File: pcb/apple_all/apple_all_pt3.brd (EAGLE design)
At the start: 56 x 65 mm, 47 parts, among them IC1 STM32F072C8T6, SW1 324_SW, SW2 324_SW, SW3 324_SW

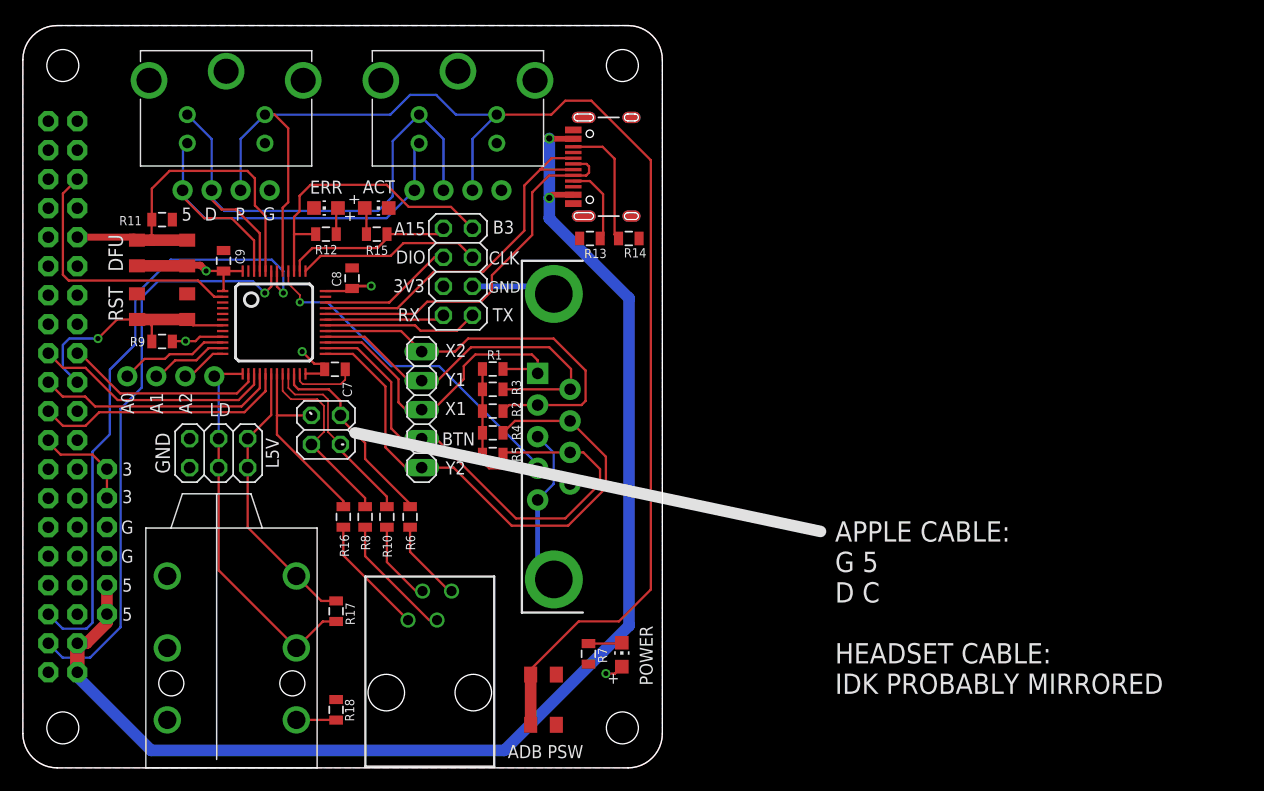
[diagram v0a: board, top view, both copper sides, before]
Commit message: updated apple_all protocol card
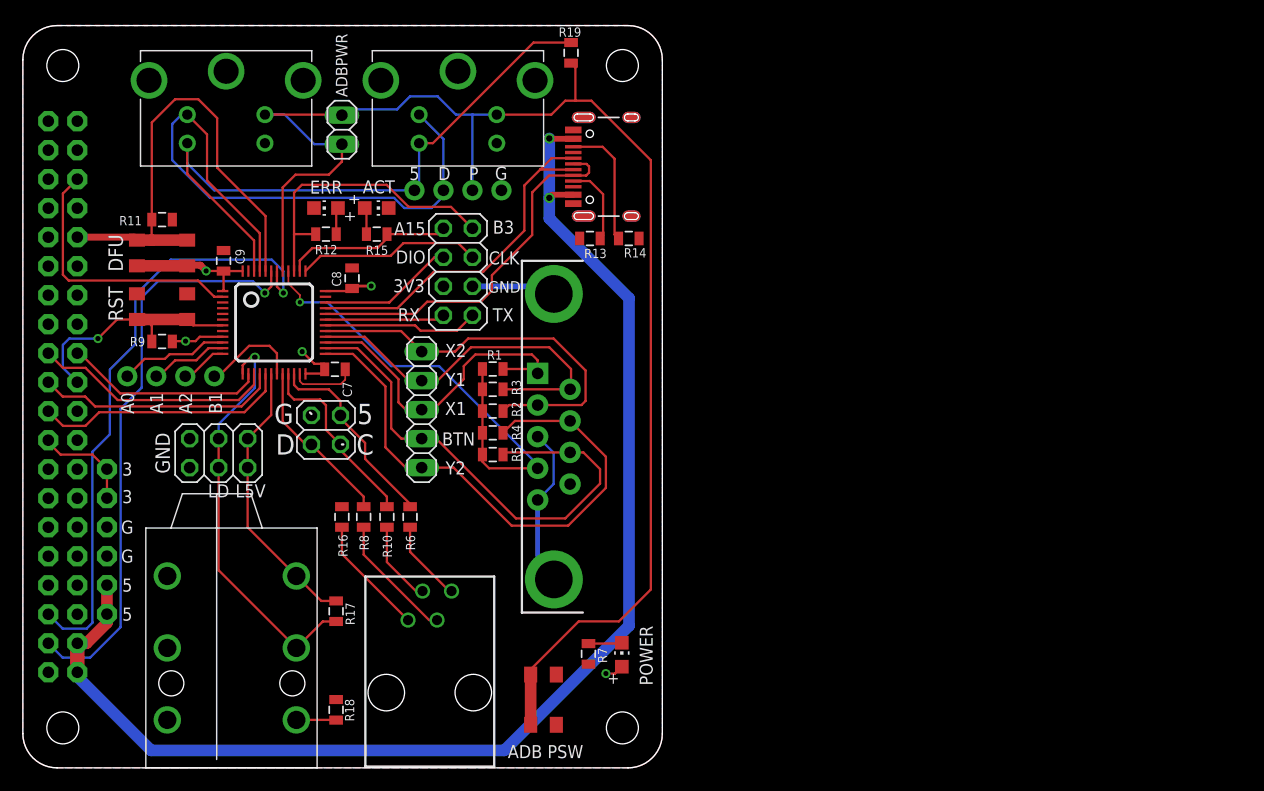
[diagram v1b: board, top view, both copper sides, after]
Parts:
- removed U$1: PINHD1X4, adafruit_changed:1X04-CLEANBIG
- added JP8: (no value), pinhead:1X02
- added R19: 2K, SparkFun-Passives:0805
- R10, R16, R6, R8: value 50 -> 200
- moved R8 0.13 mm to (29.8, 22.0)
- moved R16 0.13 mm to (27.9, 22.0)
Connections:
- removed net N$30: IC1.19, JP5.1, R16.1
- new net N$11: IC1.19, U$10.4
- net GND: now also JP5.1, R16.1; no longer U$1.1
- net N$3: now also R19.2; no longer U$1.4
- net N$41: no longer U$10.4
- net N$43: no longer U$1.3
- net N$46: now also JP8.1, JP8.2, R19.1; no longer U$1.2
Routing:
- net N$30: track 17.1 -> 0.00 mm
- net N$3: track 42.3 -> 57.5 mm
- net N$18: track 32.7 -> 42.4 mm
- net N$11: track 0.00 -> 8.66 mm
- net N$43: track 50.2 -> 55.1 mm
- net N$46: track 124.0 -> 126.5 mm
- net N$41: track 33.8 -> 36.1 mm, vias 0 -> 1
- net N$25: track 16.9 -> 14.9 mm
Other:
- board text added: "ADBPWR"
- board text added: "B1"
- board text added: "C"
- board text added: "PT4 dekuNukem DEC2022"
- board text removed: "APPLE CABLE: G 5 D C HEADSET CABLE: IDK PROBABLY MIRRORED"
- board text removed: "PT3 dekuNukem JUL2022"

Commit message: added resistors on lisa pins
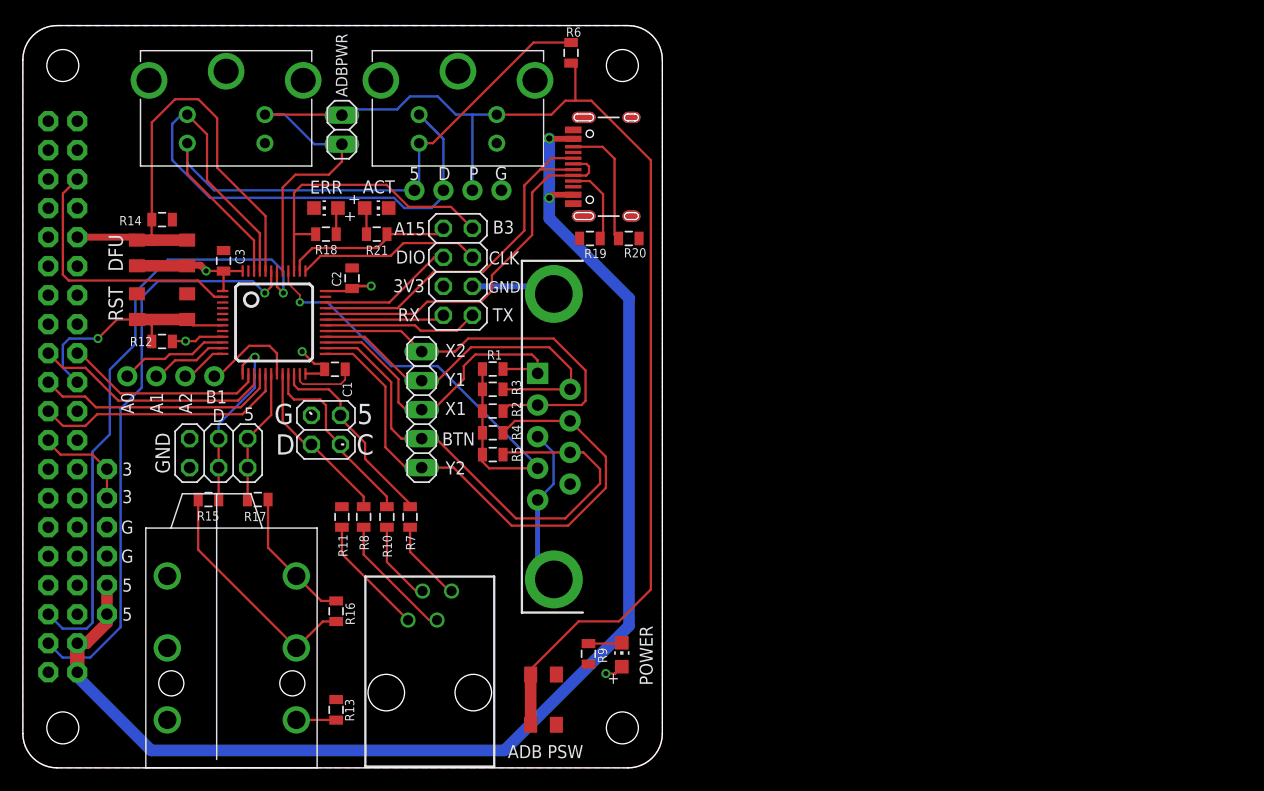
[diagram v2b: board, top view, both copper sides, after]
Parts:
- removed J4: (no value), SparkFun-Connectors:USB-C-16P
- removed U$10: PINHD1X4, adafruit_changed:1X04-CLEANBIG
- added J1: (no value), SparkFun-Connectors:DB9
- added R20: 5.1K, SparkFun-Passives:0805
- added R21: 2K, SparkFun-Passives:0805
- added U$1: M2.5HOLE, f1c100s:M2.5HOLE
- J2: device SparkFun-Connectors:DB9 -> SparkFun-Connectors:USB-C-16P
- JP1: device adafruit_changed:2X20-BIG -> pinhead:1X05
- JP2: device pinhead:2X03 -> pinhead:1X02
- JP3: device pinhead:2X04 -> pinhead:2X02
- JP4: value AUDIO-JACK4-.25-HORIZ-TRS -> (none); device SparkFun-Connectors:AUDIO-JACK-.25-INCH-HORIZ-PTH -> adafruit_changed:2X20-BIG
- JP5: device pinhead:2X02 -> pinhead:2X03
- JP6: value (none) -> AUDIO-JACK4-.25-HORIZ-TRS; device pinhead:1X05 -> SparkFun-Connectors:AUDIO-JACK-.25-INCH-HORIZ-PTH
- JP8: device pinhead:1X02 -> pinhead:2X04
- R11: value 5.1K -> 200
- R12, R19: value 2K -> 5.1K
- R13, R17: value 5.1K -> 100
- R15: value 2K -> 100
- R16: value 200 -> 5.1K
- R18: value 100 -> 2K
- R6: value 200 -> 2K
- R7: value 2K -> 200
- R9: value 5.1K -> 2K
- U$3: value M2.5HOLE -> PINHD1X4; device f1c100s:M2.5HOLE -> adafruit_changed:1X04-CLEANBIG
- U$4: value ADB -> M2.5HOLE; device adb:DIN4 -> f1c100s:M2.5HOLE
- U$6: value M2.5HOLE -> ADB; device f1c100s:M2.5HOLE -> adb:DIN4
- U$8: value PINHD1X4 -> RJ9PTH; device adafruit_changed:1X04-CLEANBIG -> SparkFun-Retired:RJ9
- U$9: value RJ9PTH -> PINHD1X4; device SparkFun-Retired:RJ9 -> adafruit_changed:1X04-CLEANBIG
- moved SW3 51.4 mm to (12.2, 45.1), turned to 180 degrees
- moved U$3 49.2 mm to (38.1, 50.6), turned to 180 degrees
- moved U$2 49.0 mm to (52.5, 3.50)
- moved SW1 48.0 mm to (45.6, 5.97), turned to 90 degrees
- moved R13 46.9 mm to (27.4, 5.08), turned to 90 degrees
- moved R9 46.3 mm to (49.5, 9.98), turned to 90 degrees
- moved U$8 44.1 mm to (35.6, 6.59), turned to 0 degrees
- moved R6 43.0 mm to (48.0, 62.6), turned to 90 degrees
- moved R18 41.7 mm to (26.5, 46.7), turned to 0 degrees
- moved R14 40.9 mm to (12.2, 48.0), turned to 180 degrees
- moved JP6 36.1 mm to (17.0, 0.00), turned to 90 degrees
- moved U$9 35.8 mm to (13.0, 34.3)
- moved JP4 35.2 mm to (3.50, 32.5), flipped to the bottom
- moved U$6 34.6 mm to (38.1, 61.0)
- moved JP1 31.4 mm to (34.9, 31.4), flipped to the top, turned to 270 degrees
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- renumbered C7 to C1, C8 to C2, C9 to C3
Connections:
- new net N$30: JP6.RING, R15.1, R16.2
- new net N$32: JP6.TIP, R16.1, R17.1
- net +3V3: now also JP4.1, JP4.17, JP8.5, R12.2, SW3.P$2, SW3.P$3; no longer JP1.1, JP1.17, JP3.5, R9.2, SW2.P$2, SW2.P$3
- net +5V: now also J2.VBUS1, J2.VBUS2, JP4.2, JP4.4; no longer J4.VBUS1, J4.VBUS2, JP1.2, JP1.4
- net +7V: now also J1.4; no longer J2.4
- net GND: now also J1.3, J1.5, J1.G1, J1.G2, J2.GND, J2.GND2, J2.SHLD1, J2.SHLD2, J2.SHLD3, J2.SHLD4, J2.SHLD5, J2.SHLD6, J2.SHLD7, J2.SHLD8, JP3.1, JP4.14, JP4.20, JP4.25, JP4.30, JP4.34, JP4.39, JP4.6, JP4.9, JP5.2, JP8.6, R14.1, R19.2, R20.2, R9.1, SW2.P$1, SW2.P$4, U$3.1, U$6.GND, U$6.SHIELD1, U$6.SHIELD2, U$6.SHIELD3; no longer J2.3, J2.5, J2.G1, J2.G2, J4.GND, J4.GND2, J4.SHLD1, J4.SHLD2, J4.SHLD3, J4.SHLD4, J4.SHLD5, J4.SHLD6, J4.SHLD7, J4.SHLD8, JP1.14, JP1.20, JP1.25, JP1.30, JP1.34, JP1.39, JP1.6, JP1.9, JP2.1, JP2.2, JP3.6, R14.2, R16.1, R18.2, R7.1, SW3.P$1, SW3.P$4, U$4.GND, U$4.SHIELD1, U$4.SHIELD2, U$4.SHIELD3, U$8.1
- net N$1: now also J2.A5, R19.1; no longer J4.A5, R13.1
- net N$10: now also U$8.3; no longer U$9.3
- net N$11: now also U$9.4; no longer U$10.4
- net N$12: now also JP8.7; no longer JP3.7
- net N$13: now also JP4.22, R12.1, SW2.P$2, SW2.P$3; no longer JP1.22, R9.1, SW1.P$2, SW1.P$3
- net N$14: now also JP8.8; no longer JP3.8
- net N$15: now also JP8.3; no longer JP3.3
- net N$16: now also JP8.4; no longer JP3.4
- net N$17: now also JP3.2, R7.1; no longer JP5.2, R6.1
- net N$18: now also JP4.32, R14.2, SW3.P$1, SW3.P$4; no longer JP1.32, R11.2, SW2.P$1, SW2.P$4
- net N$19: now also JP3.4; no longer JP5.4
- net N$2: now also R18.2; no longer R12.2
- net N$20: now also U$8.2; no longer U$9.2
- net N$21: now also R11.2, U$8.1; no longer R16.2, U$9.1
- net N$22: now also JP4.5; no longer JP1.5
- net N$23: now also JP4.3; no longer JP1.3
- net N$24: now also JP6.SLEEVE, R13.1; no longer JP4.SLEEVE, R18.1
- net N$25: now also JP3.3; no longer JP5.3
- net N$26: now also J1.1, JP1.3; no longer J2.1, JP6.3
- net N$27: now also JP8.1, R21.1; no longer JP3.1, R15.1
- net N$28: now also R21.2; no longer R15.2
- net N$29: now also R9.2; no longer R7.2
- net N$3: now also R6.2, U$3.4, U$6.5V; no longer R19.2, U$4.5V, U$8.4
- net N$31: now also JP5.5, JP5.6, R17.2; no longer JP2.5, JP2.6, JP4.TIP, R17.1
- net N$34: now also J1.6, JP1.2; no longer J2.6, JP6.2
- net N$35: now also J1.7, JP1.5; no longer J2.7, JP6.5
- net N$36: now also J1.2, JP1.1; no longer J2.2, JP6.1
- net N$37: now also JP4.36; no longer JP1.36
- net N$38: now also U$9.1; no longer U$10.1
- net N$39: now also U$9.2; no longer U$10.2
- net N$4: now also J1.8, JP1.4; no longer J2.8, JP6.4
- net N$40: now also U$9.3; no longer U$10.3
- net N$41: now also JP5.3, JP5.4, R15.2; no longer JP2.3, JP2.4, JP4.RING, R17.2
- net N$43: now also U$3.3, U$6.ADB; no longer U$4.ADB, U$8.3
- net N$46: now also JP2.1, JP2.2, R6.1, SW1.P$2, SW1.P$3, U$3.2, U$6.PSW; no longer JP8.1, JP8.2, R19.1, SW3.P$2, SW3.P$3, U$4.PSW, U$8.2
- net N$5: now also R7.2, U$8.4; no longer R6.2, U$9.4
- net N$6: now also JP8.2, R18.1; no longer JP3.2, R12.1
- net N$7: now also J2.B5, R20.1; no longer J4.B5, R14.1
- net N$8: now also J2.A6, J2.B6; no longer J4.A6, J4.B6
- net N$9: now also J2.A7, J2.B7; no longer J4.A7, J4.B7
- net SPI_CS: now also JP4.24; no longer JP1.24
- net SPI_MISO: now also JP4.21; no longer JP1.21
- net SPI_MOSI: now also JP4.19; no longer JP1.19
- net SPI_SCK: now also JP4.23; no longer JP1.23
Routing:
- net N$30: track 0.00 -> 21.0 mm
- net N$41: track 36.1 -> 15.9 mm
- net N$31: track 24.7 -> 11.9 mm
- net N$32: track 0.00 -> 12.1 mm
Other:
- board text removed: "L5V"
- board text removed: "LD"
